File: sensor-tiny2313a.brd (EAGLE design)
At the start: 56 x 39 mm, 34 parts, among them IC1 TINY2313-*P*, IC2 L6920, K1 68611014422, M1 NRF24L01P-M, M2 DHT22, Q1 BC847CSMD

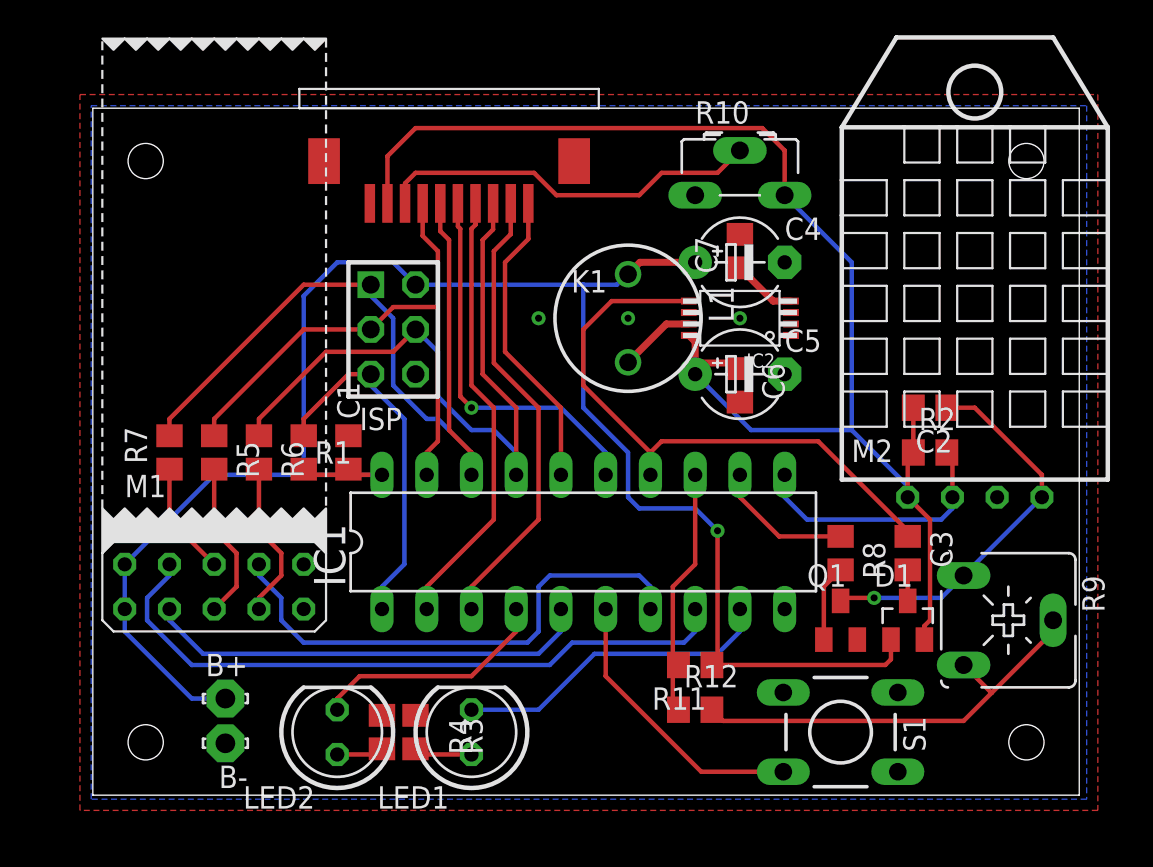
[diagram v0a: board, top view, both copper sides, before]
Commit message: removed really complicating lcd from small version, layouted single sided pcb
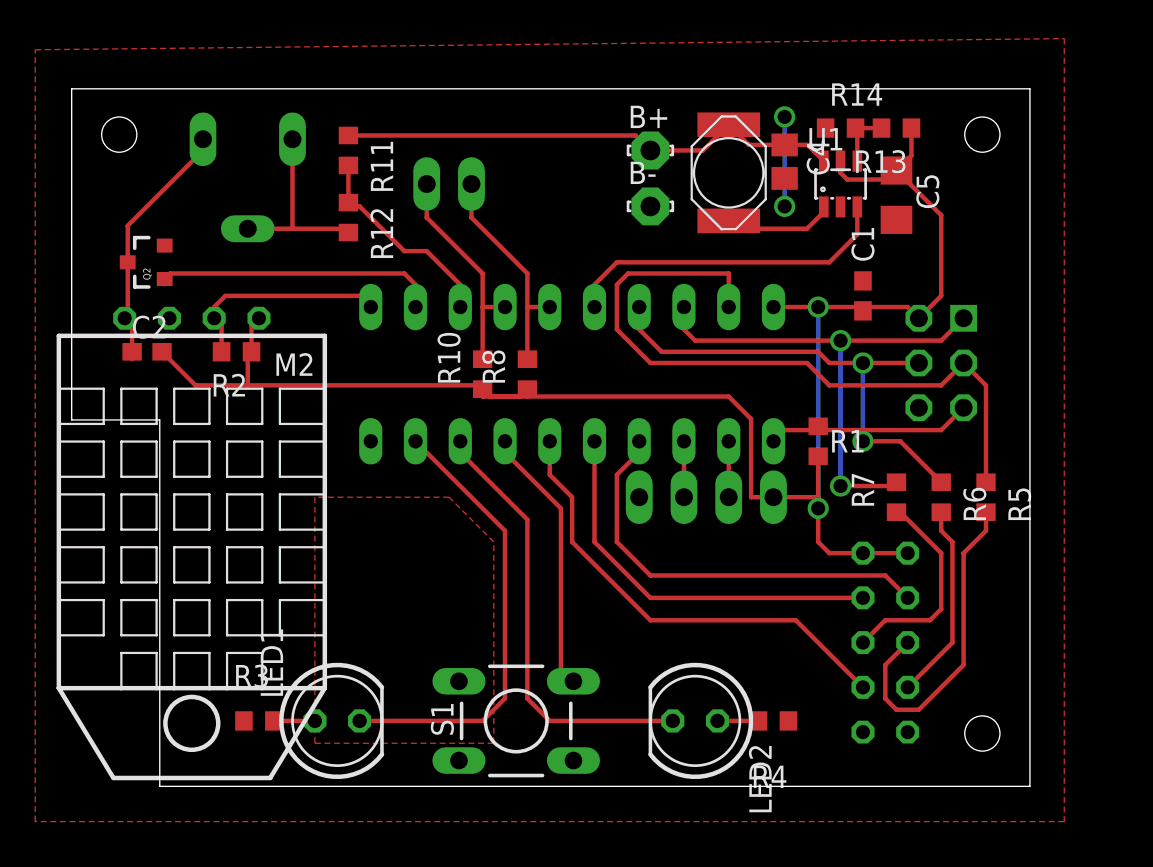
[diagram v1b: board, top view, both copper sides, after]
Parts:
- removed C3, C7: 100n, rcl:C0805
- removed C6: 1u, rcl:C0805
- removed D1: BAT54S, diode:SOT23
- removed IC2: L6920, l6920:TSSOP8
- removed K1: 68611014422, Wuerth_Elektronik_eiCan_03_ZIF_Connectors_Flat_Flexible_Cable:68611014422
- removed Q1: BC847CSMD, transistor-npn:SOT23
- added JP1: I2C, pinhead-mod:1X02
- added JP3: serial, pinhead-mod:1X04
- added Q2: IRLML2502, xmaker:SOT23-3
- added R13: 470k, rcl:R0603
- added R14: 270k, rcl:R0603
- added U1: MCP1640C, karlnet-parts:SOT23-6
- C1, C2: device rcl:C0805 -> rcl:C0603
- C4: value 47u -> 4u7; device rcl:E5-5 -> rcl:C0805
- C5: value 47u -> 22u; device rcl:E5-5 -> rcl:C1206
- L1: value 10u -> 4u7; device fastron_07HCP:FASTRON_07HCP_INDUCTOR -> inductor-Fastron:PISG
- LED1: value RT LC -> GR LC
- LED2: value GR LC -> RT LC
- R1, R11, R12, R2, R5, R6, R7: device rcl:R0805 -> rcl:R0603
- R10: value 10K -> 4k7; device pot:CA6H -> rcl:R0603
- R3: value 510 -> 470; device rcl:R0805 -> rcl:R0603
- R4: value 470 -> 510; device rcl:R0805 -> rcl:R0603
- R8: value 680 -> 4k7; device rcl:R0805 -> rcl:R0603
- U$2: value SP6062 -> SP6029TOP; device strapubox:SP6062 -> strapubox:SP6029T
- moved R9 49.8 mm to (10.8, 36.2), flipped to the bottom, turned to 180 degrees
- moved M2 45.6 mm to (7.62, 28.6), turned to 180 degrees
- moved C2 44.6 mm to (5.08, 26.7), turned to 0 degrees
- moved R5 43.9 mm to (52.7, 18.4)
- moved R7 41.4 mm to (47.6, 18.4)
- moved R2 39.8 mm to (10.2, 26.7), turned to 180 degrees
- moved B+ 39.4 mm to (33.7, 38.1), turned to 0 degrees
- moved B- 38.9 mm to (33.7, 34.9), turned to 0 degrees
- moved R6 38.8 mm to (50.2, 18.4)
- moved M1 38.2 mm to (47.0, 10.2), flipped to the bottom, turned to 270 degrees
- moved R11 35.2 mm to (16.5, 38.1), turned to 270 degrees
- moved R12 34.2 mm to (16.5, 34.3), turned to 270 degrees
- moved ISP 31.2 mm to (50.2, 26.0), flipped to the bottom
- moved C1 30.5 mm to (45.7, 29.8)
- moved R1 29.2 mm to (43.2, 21.6)
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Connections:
- net N$3 renamed RSCK
- net N$4 renamed RDI
- net N$5 renamed RDO
- net PA2 renamed !RESET
- net PB1 renamed AIN1
- net PD5 renamed LED1
- net PD6 renamed ICP1
- removed net +5V: C2.2, C5.+, C6.1, D1.2, IC2.8, K1.9, M2.1, R10.E, R2.1
- removed net N$10: IC2.7, L1.2
- removed net N$11: C7.1, IC2.4
- removed net N$12: K1.8, R10.S
- removed net N$14: C3.2, D1.3
- removed net N$6: Q1.1, R8.2
- removed net PA0: IC1.5, M1.CE
- removed net PA1: IC1.4, LED2.K
- removed net PB0: IC1.12, R8.1
- removed net PB2: C3.1, IC1.14, IC2.5
- removed net PB3: IC1.15, K1.5
- removed net PB4: IC1.16, K1.1
- removed net PB5: IC1.17, ISP.4, K1.3, R6.1
- removed net PB6: IC1.18, ISP.1, K1.6, R7.2
- removed net PB7: IC1.19, ISP.3, K1.7, R5.1
- removed net PD0: IC1.2, K1.4
- removed net PD1: IC1.3, K1.2
- removed net PD2: IC1.6, S1.2
- removed net PD3: IC1.7, M1.IRQ
- removed net PD4: IC1.8, M1.CSN
- new net DHTON: IC1.12, Q2.1
- new net DI: IC1.17, ISP.4, R6.1
- new net DO: IC1.18, ISP.1, R7.2
- new net LED2: IC1.8, LED2.K
- new net N$8: L1.1, U1.1
- new net N$9: R13.2, R14.2, U1.4
- new net PWRON: IC1.16, U1.3
- new net RFCE: IC1.4, M1.CE
- new net RFCSN: IC1.5, M1.CSN
- new net RFIRQ: IC1.6, M1.IRQ
- new net RXD: IC1.2, JP3.2
- new net SCK: IC1.19, ISP.3, R5.1
- new net SCL: IC1.15, JP1.1, R8.2
- new net SDA: IC1.14, JP1.2, R10.2
- new net SW1: IC1.7, S1.2
- new net TXD: IC1.3, JP3.3
- new net VBAT: B+.MP, C4.1, L1.2, R11.1, U1.6
- net GND: now also C4.2, C5.2, JP3.4, Q2.2, R14.1, U1.2; no longer C4.-, C5.-, C6.2, C7.2, IC2.1, IC2.6, K1.10, Q1.2, R10.A
- net N$2: now also Q2.3; no longer Q1.3
- net VCC: now also C2.2, C5.1, JP3.1, M2.1, R10.1, R13.1, R2.1, R8.1, U1.5; no longer B+.MP, C4.+, D1.1, L1.1, R11.1
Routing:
- net +5V: track 78.2 -> 0.00 mm
- net PB6: track 45.4 -> 0.00 mm
- net SCK: track 0.00 -> 39.9 mm
- net PB5: track 39.8 -> 0.00 mm
- net PD4: track 37.9 -> 0.00 mm
- net PB2: track 33.8 -> 0.00 mm
- net PB7: track 32.3 -> 0.00 mm
- net PD3: track 29.8 -> 0.00 mm
- net DO: track 0.00 -> 29.5 mm, vias 0 -> 2
- net VBAT: track 0.00 -> 28.8 mm
- net DI: track 0.00 -> 27.8 mm, vias 0 -> 2
- net RFIRQ: track 0.00 -> 26.2 mm
- net PD1: track 26.1 -> 0.00 mm
- net PA0: track 25.4 -> 0.00 mm
- net PD0: track 25.2 -> 0.00 mm
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- added copper zone on layer 1, net N$3
- removed copper zone on layer 16, net GND
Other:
- board size 56 x 39 mm -> 54.4 x 39.6 mm

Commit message: changed irlml* parts to own library with better footprint
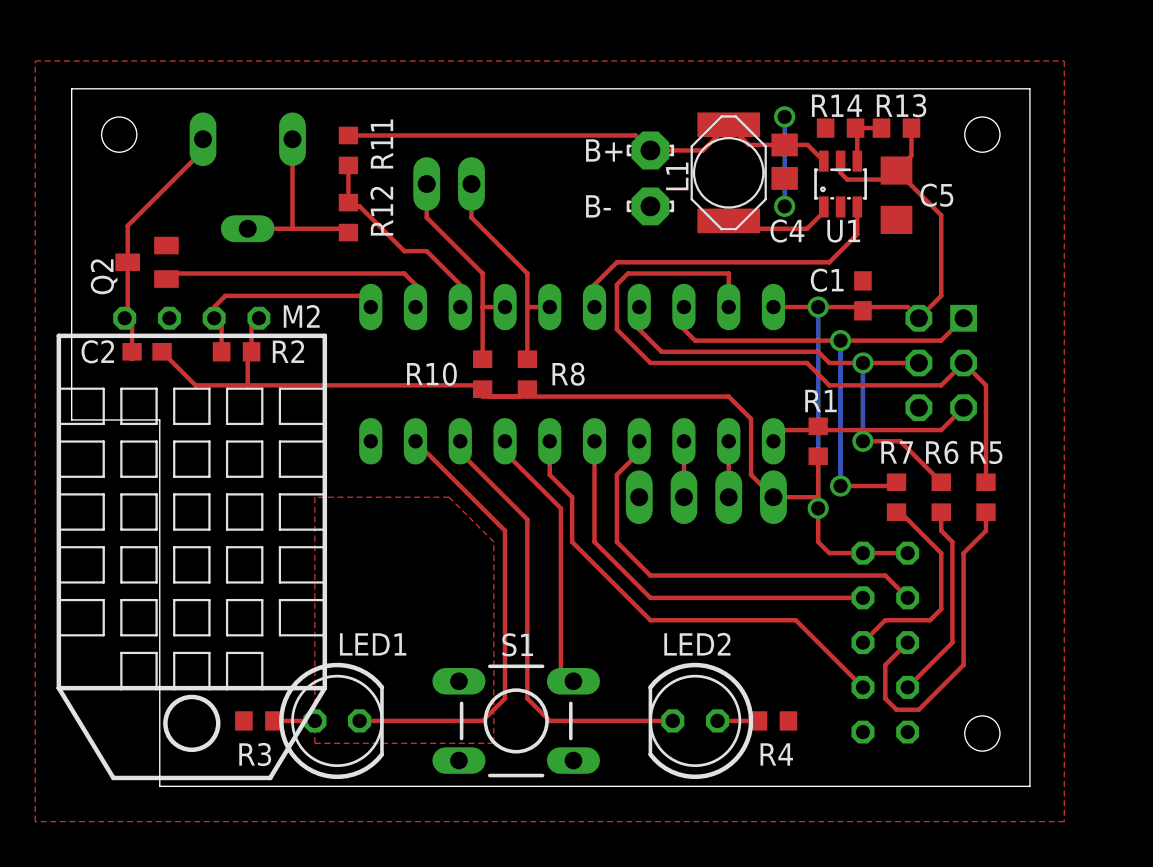
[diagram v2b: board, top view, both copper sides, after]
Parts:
- Q2: device xmaker:SOT23-3 -> mosfet:MICRO3
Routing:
- net VCC: track 97.8 -> 97.1 mm

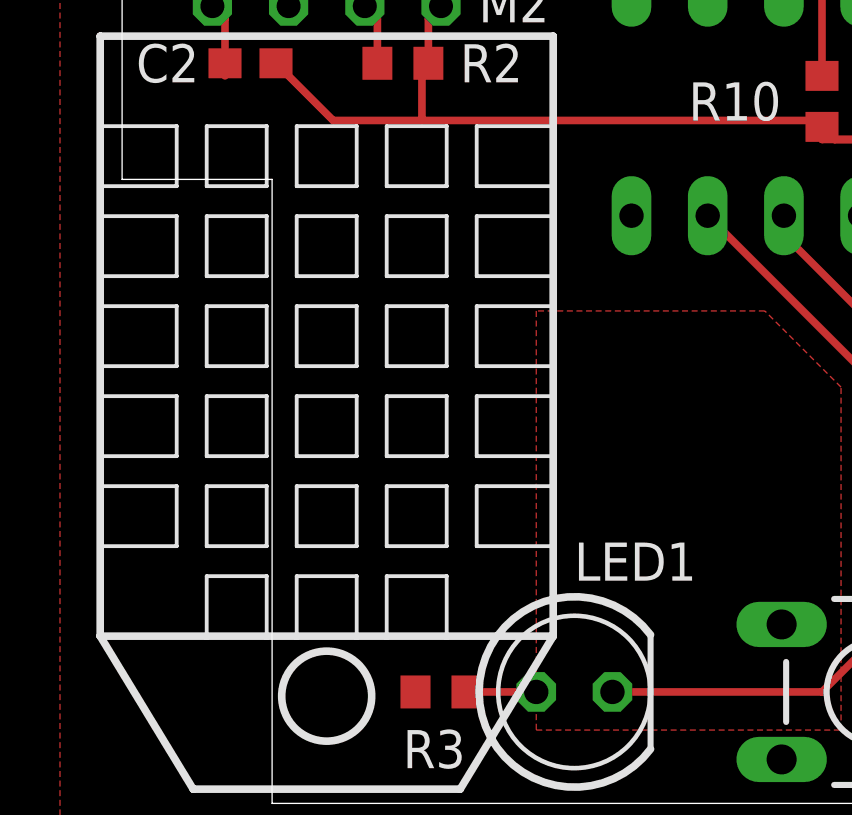
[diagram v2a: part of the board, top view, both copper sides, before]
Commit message: cc-by-sa license
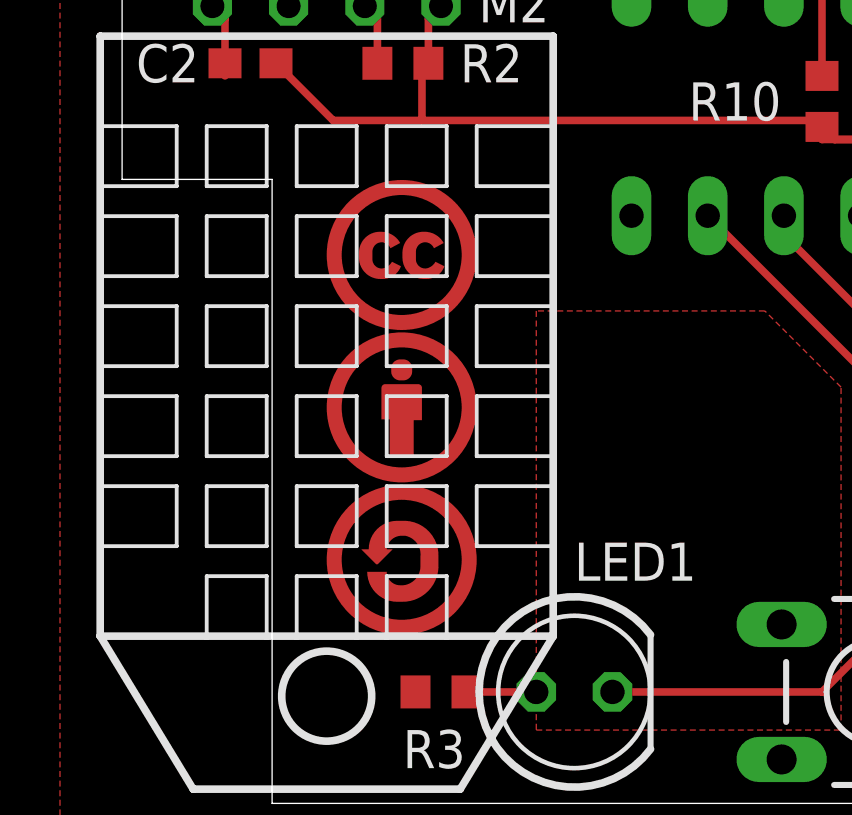
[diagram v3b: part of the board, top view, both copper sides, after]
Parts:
- added U$1: CC-TOP-HALF, creative-commons:CC_TOP_HS
- added U$3: BY-TOP-HALF, creative-commons:BY_TOP_HS
- added U$4: SA-TOP-HALF, creative-commons:SA_TOP_HS
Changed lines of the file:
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@@
 <attribute name="VALUE" x="41.91" y="15.24" size="1.27" layer="28" rot="MR0"/>
 </element>
+<element name="U$1" library="creative-commons" package="CC_TOP_HS" value="CC-TOP-HALF" x="7.62" y="17.78"/>
+<element name="U$3" library="creative-commons" package="BY_TOP_HS" value="BY-TOP-HALF" x="7.62" y="12.7"/>
+<element name="U$4" library="creative-commons" package="SA_TOP_HS" value="SA-TOP-HALF" x="7.62" y="7.62"/>
 </elements>
 <signals>

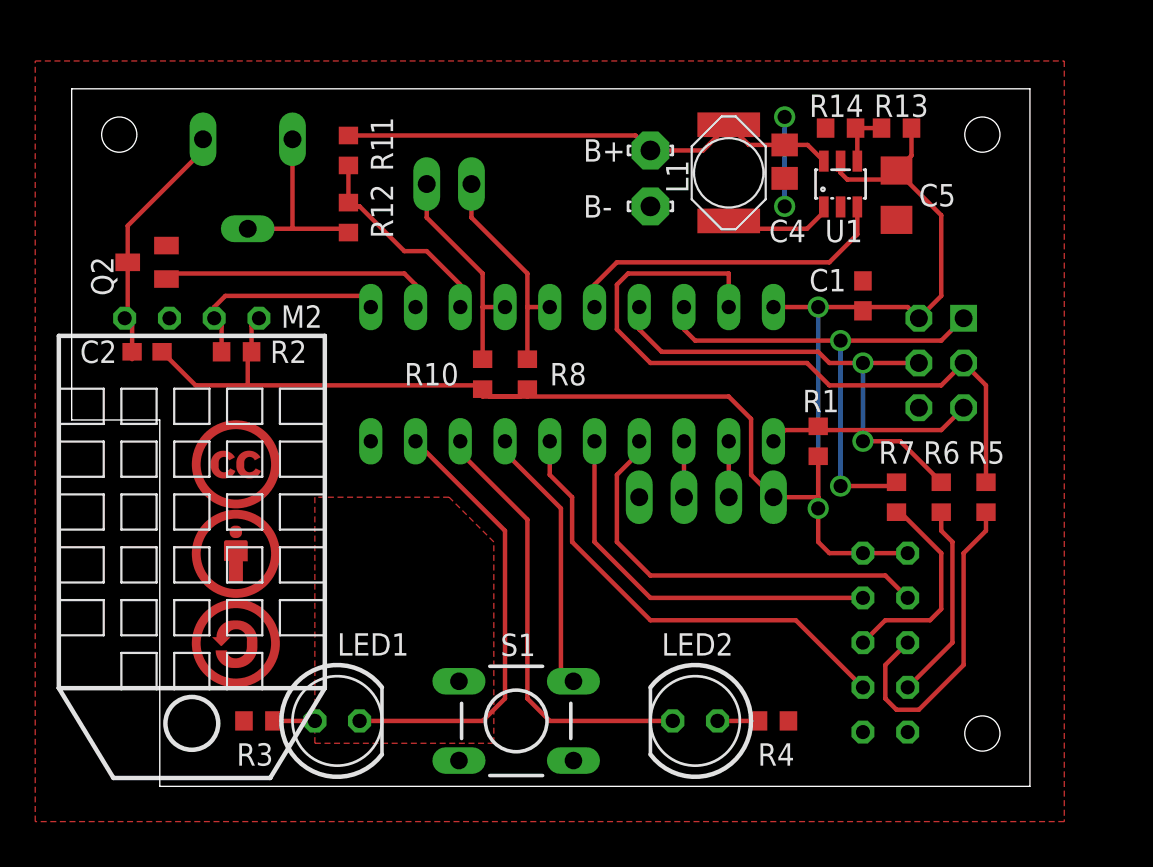
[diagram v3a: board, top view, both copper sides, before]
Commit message: attiny so20 package
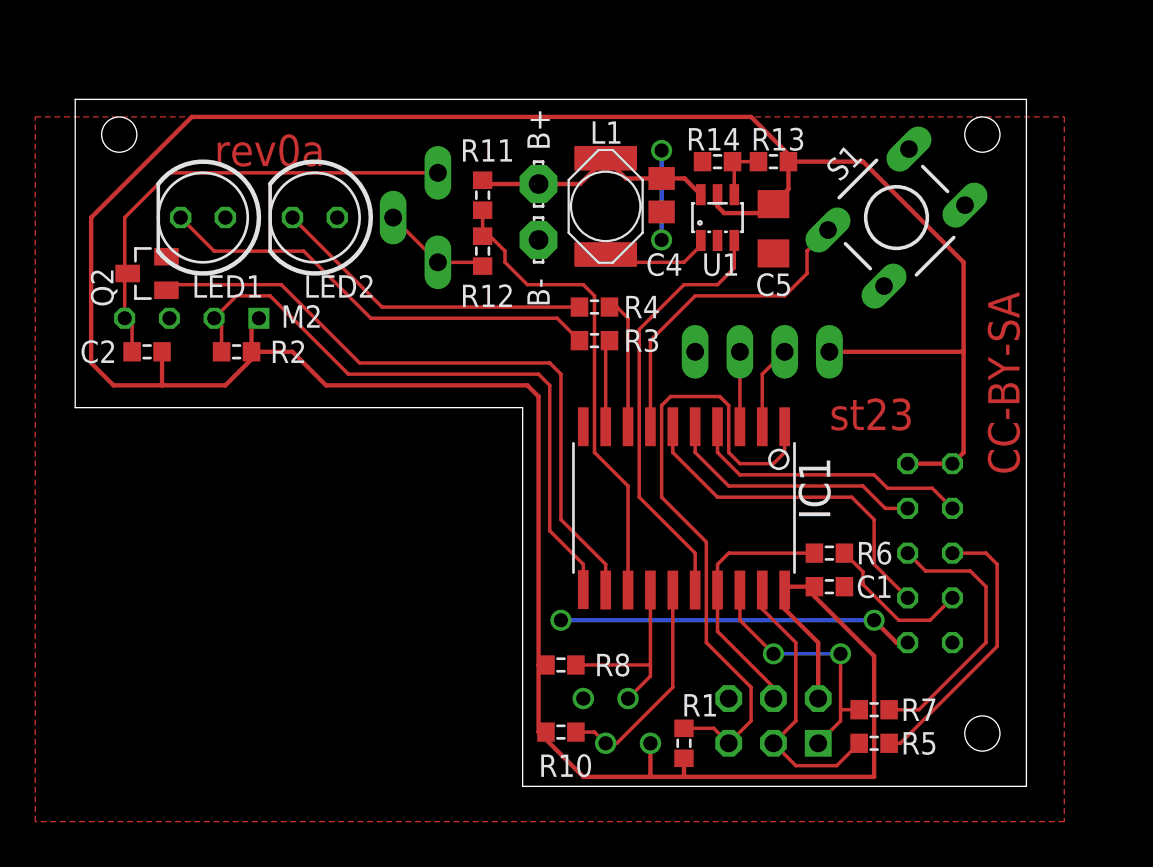
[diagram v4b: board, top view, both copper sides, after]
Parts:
- removed JP1: I2C, pinhead-mod:1X02
- removed JP3: serial, pinhead-mod:1X04
- added X1: I2C, con-amp-micromatch:MICROMATCH-4
- added X2: serial, pinhead-mod:1X04
- IC1: value TINY2313-*P* -> TINY2313-*S*; device avr-7:DIL20 -> avr-7:SO20L$
- M2: value DHT22 -> DHT22-NP; device modules:DHT22 -> modules:DHT22-NOPRINT
- R9: device pot:CA6V -> pot:CA6H
- U$1: value CC-TOP-HALF -> CC-TPLACE-HALF; device creative-commons:CC_TOP_HS -> creative-commons:CC_TPLACE_HS
- U$3: value BY-TOP-HALF -> BY-TPLACE-HS; device creative-commons:BY_TOP_HS -> creative-commons:BY_TPLACE_HS
- U$4: value SA-TOP-HALF -> SA-TPLACE-HALF; device creative-commons:SA_TOP_HS -> creative-commons:SA_TPLACE_HS
- moved LED2 35.8 mm to (14.6, 34.3)
- moved S1 35.8 mm to (47.6, 34.3), turned to 45 degrees
- moved LED1 29.6 mm to (8.26, 34.3), turned to 180 degrees
- moved R3 28.8 mm to (30.5, 27.3)
- moved R4 25.6 mm to (30.5, 29.2), turned to 180 degrees
- moved U$1 25.0 mm to (31.8, 24.1), flipped to the bottom
- moved ISP 22.4 mm to (40.6, 5.71), turned to 0 degrees
- moved U$3 21.7 mm to (26.0, 24.1), flipped to the bottom
- moved U$4 20.8 mm to (20.3, 24.1), flipped to the bottom
- moved R10 20.8 mm to (28.6, 5.08), turned to 0 degrees
- moved R1 18.8 mm to (35.6, 4.45)
- moved C1 16.6 mm to (43.8, 13.3), turned to 0 degrees
- moved R8 16.6 mm to (28.6, 8.89), turned to 0 degrees
- moved R5 15.3 mm to (46.4, 4.45), turned to 0 degrees
- moved R7 12.1 mm to (46.4, 6.35), turned to 180 degrees
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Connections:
- removed net N$13: LED1.A, R3.1
- new net N$3: LED1.K, R3.2
- net GND: now also LED1.A, LED2.A, X1.4, X2.4; no longer JP3.4, R3.2, R4.2
- net LED1: now also R3.1; no longer LED1.K
- net LED2: now also R4.1; no longer LED2.K
- net N$1: now also LED2.K, R4.2; no longer LED2.A, R4.1
- net RXD: now also X2.2; no longer JP3.2
- net SCL: now also R10.2, X1.3; no longer JP1.1, R8.2
- net SDA: now also R8.2, X1.2; no longer JP1.2, R10.2
- net SW1: now also S1.1; no longer S1.2
- net TXD: now also X2.3; no longer JP3.3
- net VCC: now also X1.1, X2.1; no longer JP3.1
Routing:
- net VCC: track 97.1 -> 188.7 mm, vias 2 -> 0
- net N$3: track 0.00 -> 25.5 mm
- net !RESET: track 11.8 -> 36.8 mm
- net SCK: track 39.9 -> 15.9 mm
- net ICP1: track 12.5 -> 36.4 mm
- net DHTON: track 15.8 -> 37.9 mm
- net LED1: track 25.5 -> 4.98 mm
- net GND: track 5.08 -> 25.3 mm, vias 2 -> 4
- net LED2: track 25.0 -> 7.48 mm
- net N$1: track 2.32 -> 18.4 mm
- net AIN1: track 12.1 -> 27.1 mm
- net VBAT: track 28.8 -> 13.9 mm
- net DO: track 29.5 -> 14.9 mm
- net DI: track 27.8 -> 14.7 mm, vias 2 -> 0
- net N$2: track 14.7 -> 27.5 mm
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- removed copper zone on layer 1, net N$3
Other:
- board size 54.4 x 39.6 mm -> 54 x 39 mm
- board text added: ">BN"
- board text added: ">BR"
- board text added: "CC-BY-SA"
